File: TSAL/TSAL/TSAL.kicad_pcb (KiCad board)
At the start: 2 copper layers, 161 x 29 mm, 51 parts, among them J1 CONN_01X04, U1 L78S05CV-DG, U2 LM555N

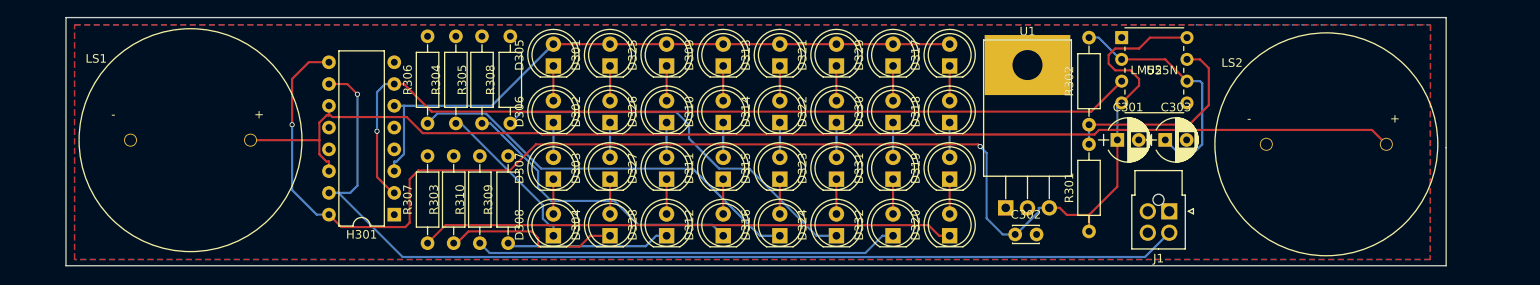
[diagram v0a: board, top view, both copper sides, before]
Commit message: Need to correct Bay Area DFM warnings on TSAL. Brake Light passed and ready to be sent.
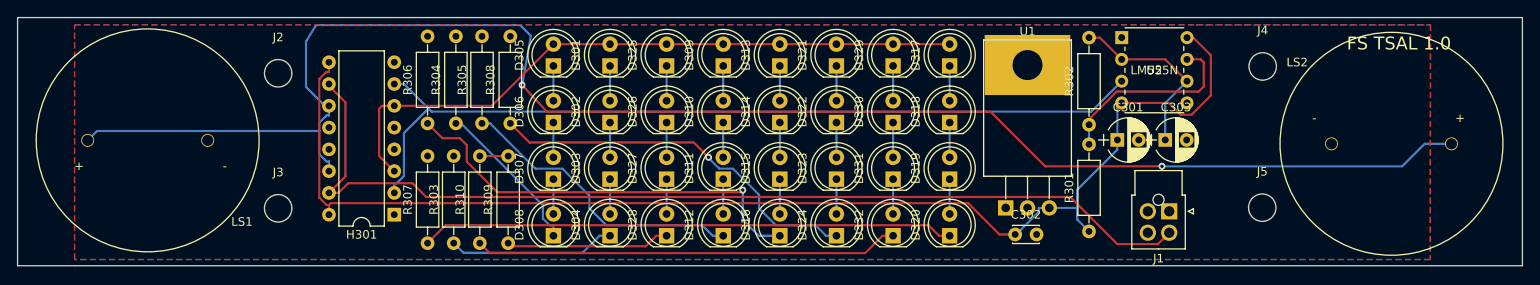
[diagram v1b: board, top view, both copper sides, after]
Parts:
- added J2: Conn_01x01, Mounting_Holes:MountingHole_3.2mm_M3, F.Cu at (65.3, 90.9)
- added J3: Conn_01x01, Mounting_Holes:MountingHole_3.2mm_M3, F.Cu at (65.3, 106.7)
- added J4: Conn_01x01, Mounting_Holes:MountingHole_3.2mm_M3, F.Cu at (180.2, 90.1)
- added J5: Conn_01x01, Mounting_Holes:MountingHole_3.2mm_M3, F.Cu at (180.1, 106.6)
- moved LS2 7.60 mm to (195.2, 99.2)
- moved LS1 5.00 mm to (50.1, 98.8), turned to 180 degrees
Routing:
- net /RTDS_H: track 142.2 -> 192.4 mm, vias 0 -> 2
- net +5V: track 166.0 -> 147.4 mm, vias 2 -> 0
- net Net-(C303-Pad1): track 28.1 -> 21.4 mm
- net /SIG_RTDS: track 120.5 -> 116.3 mm, vias 1 -> 0
- net Net-(H301-Pad2): track 102.7 -> 99.3 mm, vias 1 -> 0
- net GND: track 0.00 -> 3.30 mm
- net Net-(D316-Pad1): track 47.5 -> 49.9 mm, vias 0 -> 1
- net /OSC: track 76.0 -> 77.7 mm
- net Net-(R301-Pad2): track 24.5 -> 22.8 mm
- net Net-(D304-Pad1): track 20.7 -> 19.5 mm
- net Net-(D324-Pad1): track 45.5 -> 44.4 mm, vias 0 -> 1
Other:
- board size 161 x 29 mm -> 175.6 x 29 mm
- net class Default: via_dia 0.6 -> 0.8
- rule trace_min: 0.2 -> 0.25
- board text added: "FS TSAL 1.0"

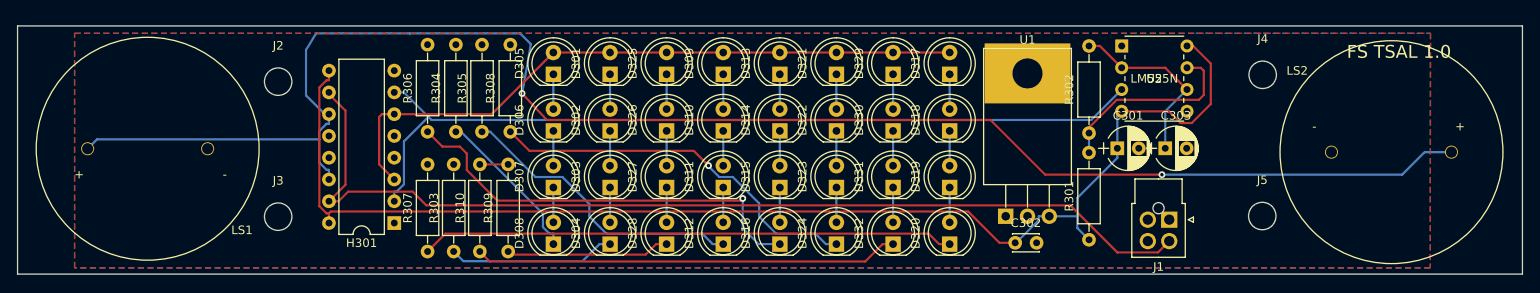
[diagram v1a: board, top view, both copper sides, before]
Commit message: Updated TSAL. passed DFM
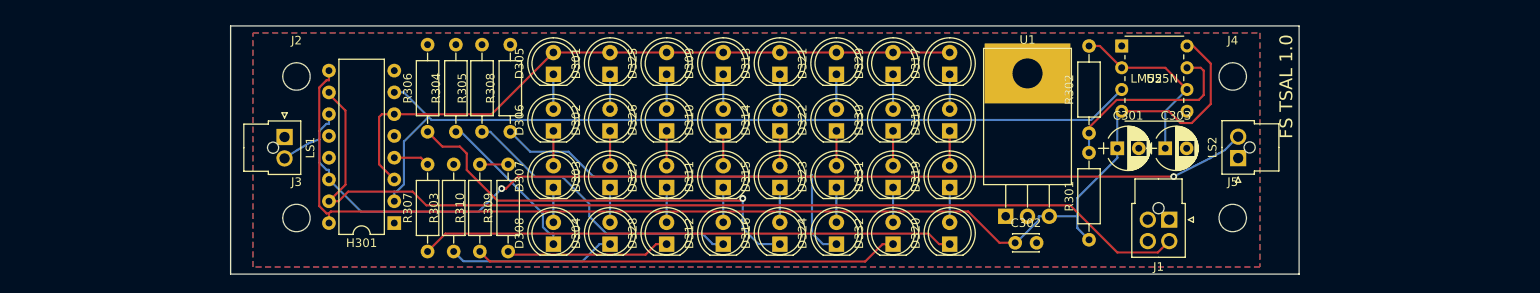
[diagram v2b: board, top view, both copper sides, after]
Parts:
- LS1, LS2: footprint FSfootprints:RTDS_H -> Connectors_Molex:Molex_NanoFit_1x02x2.50mm_Straight
- moved LS2 17.9 mm to (177.3, 99.8), turned to 90 degrees
- moved LS1 16.0 mm to (66.1, 97.4), turned to 270 degrees
- moved J4 3.50 mm to (176.7, 90.3)
- moved J5 3.45 mm to (176.7, 106.8)
- moved J2 2.22 mm to (67.5, 90.3)
- moved J3 2.14 mm to (67.5, 106.8)
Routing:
- net /RTDS_H: track 192.4 -> 124.5 mm
- net GND: track 3.30 -> 7.51 mm
- net Net-(D324-Pad1): track 44.4 -> 47.6 mm, vias 1 -> 0
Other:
- board size 175.6 x 29 mm -> 124.7 x 29 mm

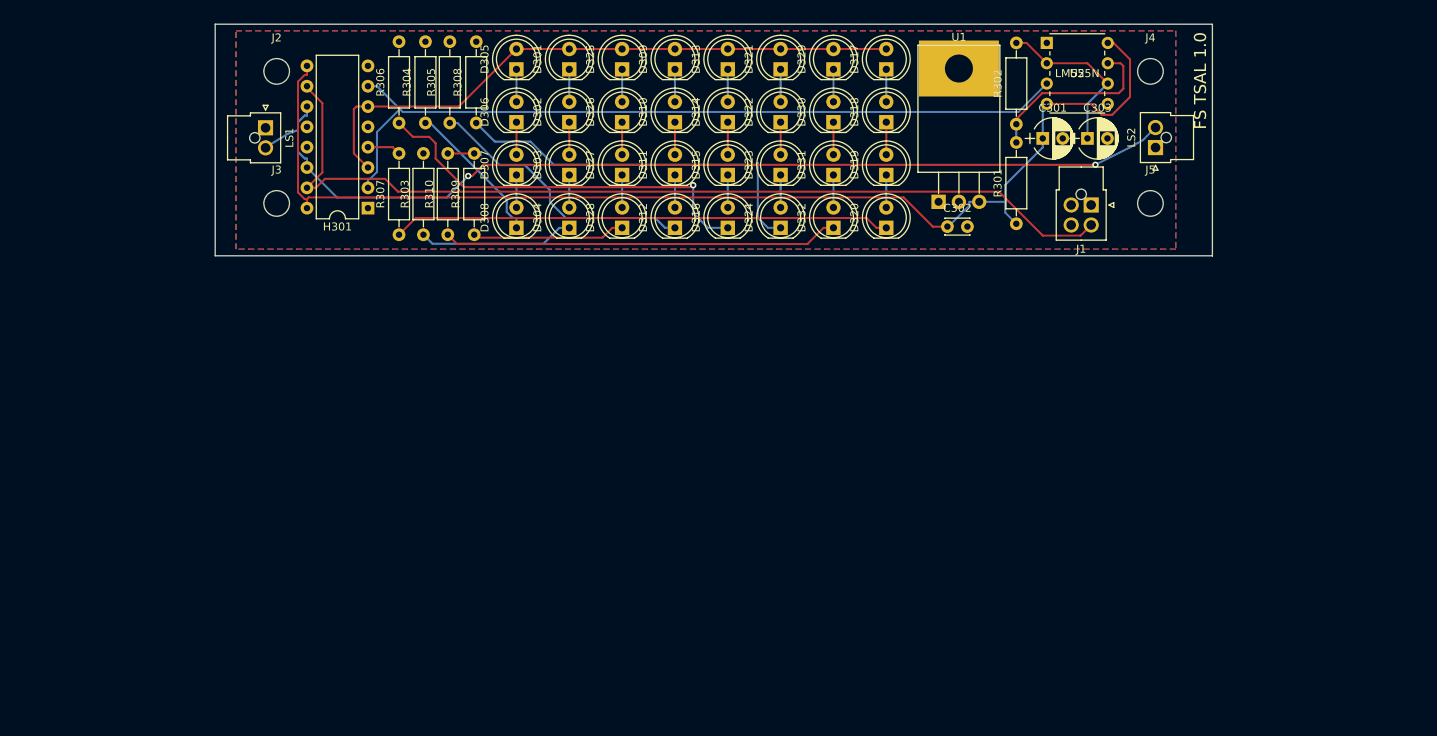
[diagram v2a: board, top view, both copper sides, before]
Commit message: resdesigned tsal. It is circular, much like fs0 tsal.
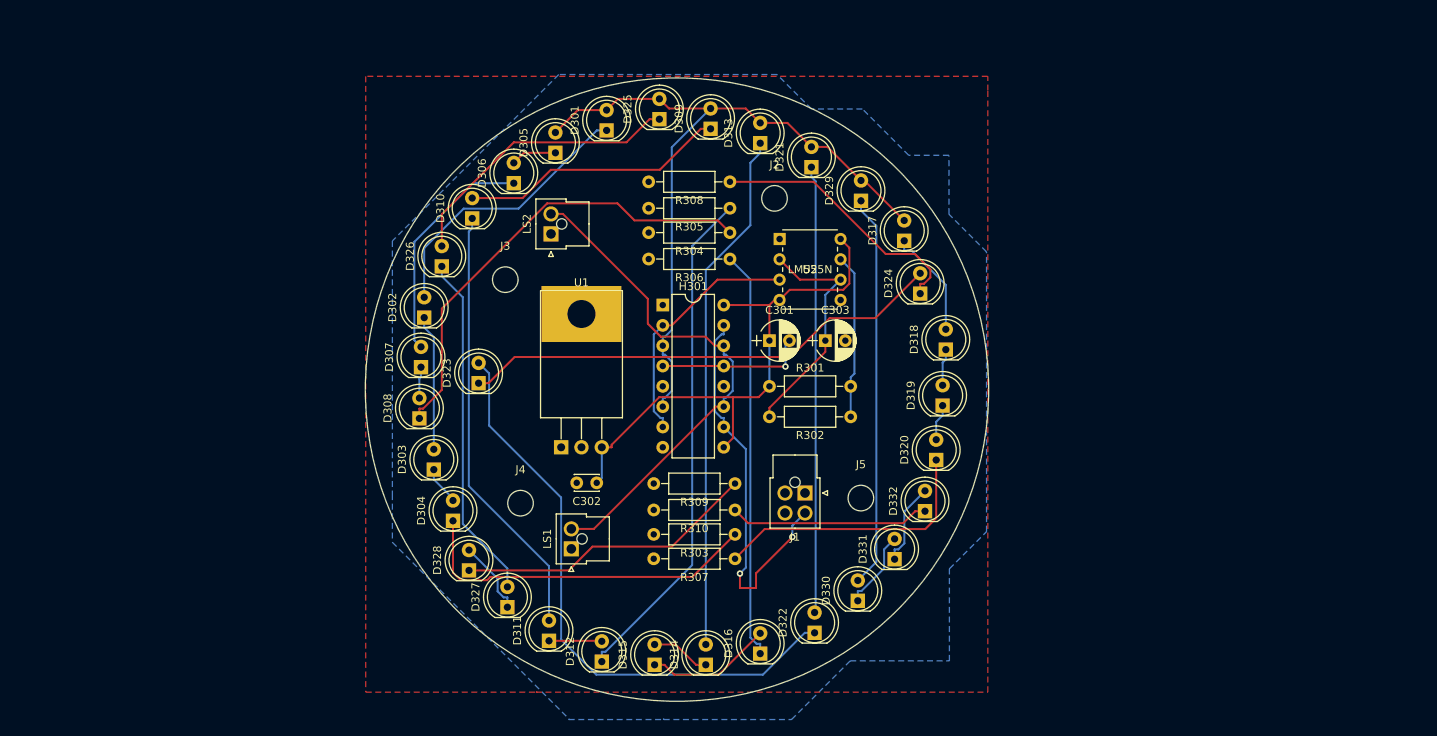
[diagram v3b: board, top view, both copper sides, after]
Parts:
- moved J4 95.5 mm to (97.9, 144.3)
- moved LS2 76.3 mm to (101.8, 110.6)
- moved D314 67.9 mm to (121.1, 164.5)
- moved LS1 65.0 mm to (104.3, 150.0), turned to 90 degrees
- moved J2 64.2 mm to (129.7, 106.2)
- moved D322 64.0 mm to (134.7, 160.5)
- moved D315 61.9 mm to (114.7, 164.5)
- moved D311 60.3 mm to (101.5, 161.5)
- moved D330 59.9 mm to (140.1, 156.5)
- moved R307 58.3 mm to (124.8, 151.2), turned to 180 degrees
- moved U1 56.3 mm to (103.0, 137.3)
- moved D327 55.9 mm to (96.3, 157.3)
- moved D312 55.0 mm to (108.1, 164.1)
- moved C302 54.3 mm to (107.5, 141.8), turned to 180 degrees
- moved R303 54.0 mm to (124.8, 148.2), turned to 180 degrees
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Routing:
- net +5V: track 147.4 -> 68.8 mm
- net Net-(D322-Pad1): track 4.06 -> 74.5 mm
- net Net-(H301-Pad2): track 99.3 -> 30.8 mm
- net /SIG_RTDS: track 116.3 -> 49.5 mm, vias 0 -> 2
- net Net-(D313-Pad1): track 4.06 -> 65.5 mm
- net /RTDS_H: track 124.5 -> 64.6 mm, vias 2 -> 0
- net Net-(D323-Pad1): track 4.06 -> 60.9 mm
- net Net-(D321-Pad1): track 4.06 -> 55.9 mm
- net Net-(D310-Pad1): track 4.06 -> 54.6 mm
- net Net-(D329-Pad1): track 4.06 -> 49.2 mm
- net Net-(D308-Pad1): track 18.4 -> 58.1 mm
- net Net-(D326-Pad1): track 4.06 -> 43.5 mm
- net Net-(D325-Pad1): track 4.06 -> 36.1 mm
- net Net-(D301-Pad1): track 4.06 -> 35.0 mm
- net Net-(D309-Pad1): track 4.06 -> 33.4 mm
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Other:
- board size 124.7 x 29 mm -> 77.9 x 77.9 mm
- board text removed: "FS TSAL 1.0"
